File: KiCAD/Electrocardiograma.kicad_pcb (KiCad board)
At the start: 2 copper layers, 56.5 x 48.1 mm, 89 parts, among them J1 54-00174, J2 Conn_01x02_Pin, J3 USB_C_Receptacle_PowerOnly_6P, J4 Conn_01x02_Pin, J5 Conn_01x02_Pin, J6 Conn_01x04_Pin, U1 INA823DT, U2 ESP32-C3-WROOM-02, U3 TLV1117-33, U4 TLV4888, U5 TLV4888, U6 TLV1117-ADJ, U7 SC6038, U8 CH224K

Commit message: cambios de placa y esquematico
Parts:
- moved C25 48.1 mm to (199.2, 61.0)
- moved R45 48.1 mm to (210.1, 63.4)
- moved R47 48.1 mm to (210.1, 66.4)
- moved R48 48.1 mm to (210.1, 69.3)
- moved R49 48.1 mm to (210.1, 72.3)
- moved C22 33.2 mm to (204.2, 65.1)
- moved C24 33.2 mm to (204.2, 71.1)
- moved C20 33.2 mm to (204.3, 59.1)
- moved C21 33.2 mm to (204.2, 62.1)
- moved D6 33.2 mm to (195.3, 50.1)
- moved R42 33.2 mm to (195.3, 54.1)
- moved C23 33.2 mm to (204.2, 68.1)
- moved C26 33.2 mm to (204.2, 54.6)
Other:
- board size 56.5 x 48.1 mm -> 67 x 50 mm

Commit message: Falta por aprobar errores en la etapa de amplificación
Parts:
- added C27: 10nF, Capacitor_SMD:C_0805_2012Metric_Pad1.18x1.45mm_HandSolder, F.Cu at (215.5, 60.9)
- added C28: 10nF, Capacitor_SMD:C_0805_2012Metric_Pad1.18x1.45mm_HandSolder, F.Cu at (215.5, 63.9)
- added C29: 10nF, Capacitor_SMD:C_0805_2012Metric_Pad1.18x1.45mm_HandSolder, F.Cu at (215.5, 66.9)
- added C30: 10nF, Capacitor_SMD:C_0805_2012Metric_Pad1.18x1.45mm_HandSolder, F.Cu at (215.5, 69.9)
- added C31: 10nF, Capacitor_SMD:C_0805_2012Metric_Pad1.18x1.45mm_HandSolder, F.Cu at (215.5, 72.9)
- added R50: 120, Resistor_SMD:R_0805_2012Metric_Pad1.20x1.40mm_HandSolder, F.Cu at (220.3, 60.8)
- R10: value 22K -> 2K67
- R11: value 33K -> 4k
- R12, R34, R36: value 100K -> 1K
- R17, R21: value 27K -> 2K67
- R19, R20, R22, R23: value 100K -> 10K
- R24: value 33K -> 1K
- R25: value 330k -> 24k
- R4: value 330k -> 33k
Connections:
- C22 pad 1: /Leveled_Signal -> Net-(C22-Pad1)
- R36 pad 2: /Leveled_Signal -> Net-(C22-Pad1)
- U4 pad 14: /Leveled_Signal -> Net-(C22-Pad1)
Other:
- outline, holes or cut-outs redrawn

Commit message: route tracing
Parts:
- R11: footprint Resistor_SMD:R_0805_2012Metric_Pad1.20x1.40mm_HandSolder -> Resistor_SMD:R_0603_1608Metric_Pad0.98x0.95mm_HandSolder
- R25: value 24k -> 1k
- moved R50 86.4 mm to (157.8, 120.5), turned to 180 degrees
- moved C26 80.9 mm to (139.6, 103.4), turned to 180 degrees
- moved C31 78.4 mm to (153.2, 120.5)
- moved C22 68.7 mm to (163.6, 120.5)
- moved C25 59.1 mm to (168.7, 111.6), turned to -90 degrees
- moved D6 54.9 mm to (146.2, 74.8), turned to 0 degrees
- moved C27 52.3 mm to (178.3, 97.6), turned to 180 degrees
- moved R42 48.7 mm to (151.4, 75.2)
- moved C20 47.7 mm to (165.8, 87.3), turned to 90 degrees
- moved R45 44.8 mm to (178.3, 95.0), turned to 180 degrees
- moved C30 40.2 mm to (213.8, 110.0)
- moved C24 39.0 mm to (205.0, 110.1)
- moved R49 37.8 mm to (209.4, 110.1)
- moved C29 35.3 mm to (213.2, 102.1)
- moved C23 34.2 mm to (204.6, 102.3)
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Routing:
- net +6.1V: track 156.5 -> 90.1 mm, vias 5 -> 2
- net Net-(C20-Pad2): track 0.00 -> 30.0 mm, vias 0 -> 3
- net Net-(C22-Pad1): track 0.00 -> 21.6 mm, vias 0 -> 2
- net Net-(D6-A): track 0.00 -> 18.1 mm
- net Net-(U1--): track 15.8 -> 0.00 mm
- net -BATT_REG: track 25.5 -> 41.1 mm, vias 33 -> 28
- net Net-(U1-+): track 13.0 -> 0.00 mm
- net +BATT: track 18.7 -> 8.14 mm
- net +3.3V: track 134.3 -> 124.3 mm
- net Net-(U5A-+): track 25.0 -> 34.5 mm
- net Net-(U4A--): track 15.1 -> 6.55 mm
- net Net-(D6-K): track 0.00 -> 7.79 mm
- net GND: track 89.7 -> 96.9 mm, vias 7 -> 6
- net Net-(U4D--): track 15.1 -> 21.7 mm
- net Net-(U6-ADJ): track 7.10 -> 12.7 mm
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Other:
- board text removed: "Añadidos Capacitores de desacople"

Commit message: Update Electrocardiograma.kicad_pcb
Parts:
- D1: value D_TVS_Dual_AAC -> TVS
- moved C28 69.3 mm to (144.2, 101.4), turned to 90 degrees
- moved C29 60.0 mm to (153.3, 106.0)
- moved C21 59.6 mm to (145.3, 94.7), turned to 180 degrees
- moved R47 58.8 mm to (150.6, 92.1), turned to 180 degrees
- moved C23 46.8 mm to (157.8, 105.9)
- moved R48 46.7 mm to (162.2, 105.9)
- moved D6 15.8 mm to (162.0, 74.3)
- moved R10 4.11 mm to (150.6, 97.4)
- moved R11 1.51 mm to (150.6, 94.7)
- moved C5 1.14 mm to (145.3, 97.3)
- moved C8 0.92 mm to (145.3, 92.1)
- moved R25 0.85 mm to (162.2, 103.4)
- moved C11 0.84 mm to (157.8, 103.4)
- moved R20 0.84 mm to (153.3, 103.4)
- moved C15 0.60 mm to (153.5, 84.3)
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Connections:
- C26 pad 2: Net-(U6-ADJ) -> unconnected-(C26-Pad2)
- R31 pad 1: +6.1V -> unconnected-(R31-Pad1)
- R31 pad 2: Net-(U6-ADJ) -> unconnected-(R31-Pad2)
- R32 pad 1: Net-(U6-ADJ) -> unconnected-(R32-Pad1)
- R32 pad 2: -BATT_REG -> unconnected-(R32-Pad2)
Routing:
- net Net-(C11-Pad2): track 0.00 -> 18.0 mm, vias 0 -> 2
- net Net-(C21-Pad2): track 0.00 -> 16.6 mm
- net Net-(D6-A): track 18.1 -> 4.28 mm
- net GND: track 96.9 -> 104.7 mm, vias 6 -> 5
- net Net-(U5C-+): track 17.1 -> 12.9 mm, vias 0 -> 2
- net /N50Hz_out: track 16.8 -> 13.1 mm, vias 0 -> 2
- net /Sensing_Out: track 12.2 -> 8.89 mm
- net Net-(U5B--): track 10.3 -> 13.4 mm
- net Net-(U5C--): track 7.40 -> 10.2 mm
- net Net-(C11-Pad1): track 18.4 -> 15.7 mm, vias 0 -> 2
- net Net-(C5-Pad2): track 17.8 -> 19.6 mm
- net Net-(D6-K): track 7.79 -> 9.23 mm
- net Net-(U5D--): track 10.8 -> 10.0 mm
- net /LPF_out: track 18.8 -> 18.5 mm, vias 2 -> 0

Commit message: Update Electrocardiograma.kicad_pcb
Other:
- outline, holes or cut-outs redrawn
- board text removed: "Falso, debe sobresalir para igualar el grosor de la carcasa"

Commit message: Update Electrocardiograma.kicad_pcb
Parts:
- moved C30 43.6 mm to (170.7, 103.1), turned to -90 degrees
- moved R49 43.2 mm to (166.8, 103.4)
- moved C24 39.4 mm to (166.8, 100.7)
- moved R4 5.59 mm to (168.7, 116.6)
- moved R5 3.41 mm to (171.4, 111.6), turned to 90 degrees
- moved C14 3.31 mm to (166.8, 105.9), turned to 0 degrees
- moved R1 2.42 mm to (174.5, 107.1)
- moved R2 2.16 mm to (174.5, 102.5)
- moved R24 0.14 mm to (171.4, 116.6)
- moved R48 0.08 mm to (162.2, 105.9)
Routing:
- net GND: track 104.7 -> 136.0 mm, vias 5 -> 7
- net Net-(C24-Pad2): track 0.00 -> 14.8 mm
- net -BATT_REG: track 41.1 -> 27.6 mm, vias 28 -> 29
- net Net-(U4A-+): track 13.9 -> 2.30 mm, vias 2 -> 1
- net Net-(R2-Pad2): track 0.00 -> 5.29 mm
- net Net-(R1-Pad1): track 0.00 -> 5.28 mm
- net Net-(U4B--): track 8.65 -> 13.2 mm
- net +6.1V: track 90.1 -> 94.3 mm
- net Net-(C25-Pad1): track 8.32 -> 12.0 mm
- net Net-(U5D--): track 10.0 -> 12.5 mm
- net /Sensing_Out: track 8.89 -> 7.37 mm
- net Net-(U4D-+): track 21.3 -> 20.1 mm
- net Net-(J1-Pad2): track 4.47 -> 3.49 mm
- net Net-(U4A--): track 6.55 -> 7.34 mm

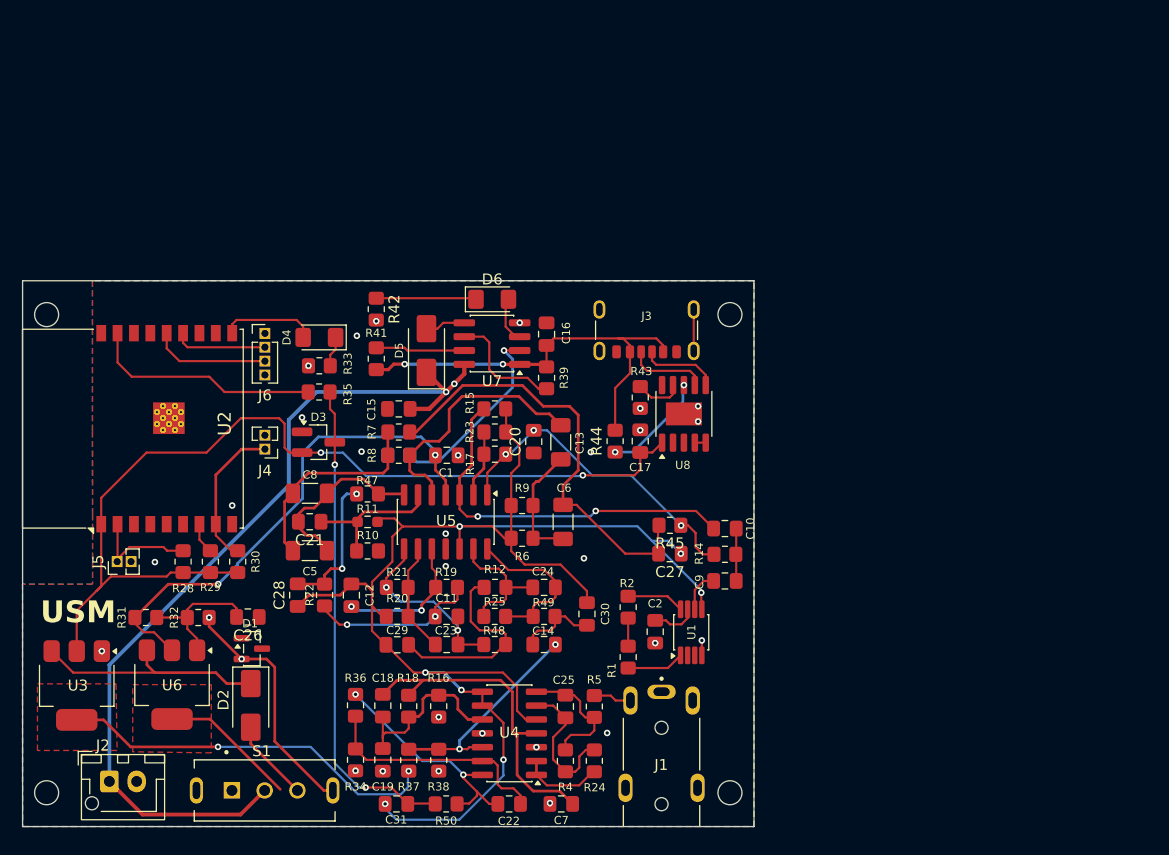
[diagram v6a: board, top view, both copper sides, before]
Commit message: Finished first PCB retracing
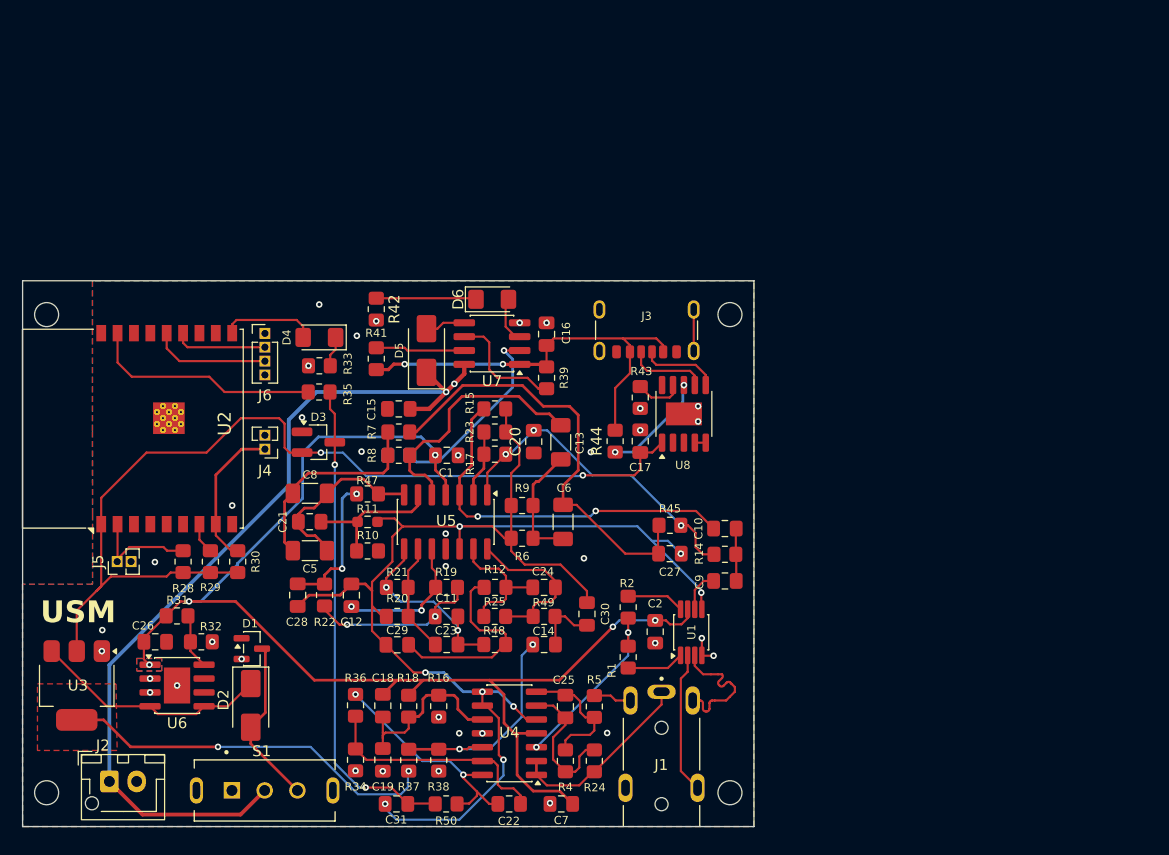
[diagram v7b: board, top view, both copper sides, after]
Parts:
- D1: value TVS -> D_TVS_Dual_AAC
- R31: value 120 -> 1k
- R32: value 470 -> 100
- U6: value TLV1117-ADJ -> ASPL4030-ADJW-R; footprint Package_TO_SOT_SMD:SOT-223-3_TabPin2 -> Package_SO:SOIC-8-1EP_3.9x4.9mm_P1.27mm_EP2.41x3.3mm
- moved C26 8.79 mm to (131.2, 105.7)
- moved R31 2.87 mm to (133.2, 103.3)
- moved R32 2.24 mm to (135.4, 105.7)
- moved U6 0.47 mm to (133.2, 109.7), turned to 0 degrees
- turned C14 to 180 degrees
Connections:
- C26 pad 2: unconnected-(C26-Pad2) -> +6.1V
- R31 pad 1: unconnected-(R31-Pad1) -> +6.1V
- R31 pad 2: unconnected-(R31-Pad2) -> Net-(U6-FB)
- R32 pad 1: unconnected-(R32-Pad1) -> Net-(U6-FB)
- R32 pad 2: unconnected-(R32-Pad2) -> -BATT_REG
- U6 pad 1: Net-(U6-ADJ) -> +6.1V
- U6 pad 2: +6.1V -> -BATT_REG
- U6 pad 3: Net-(D2-K) -> -BATT_REG
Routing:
- net +6.1V: track 94.3 -> 118.2 mm, vias 2 -> 5
- net -BATT_REG: track 27.6 -> 6.52 mm, vias 29 -> 37
- net Net-(U4A-+): track 2.30 -> 16.3 mm, vias 1 -> 2
- net Net-(U1--): track 0.00 -> 13.0 mm
- net Net-(U1-+): track 0.00 -> 12.9 mm
- net Net-(U6-ADJ): track 12.7 -> 0.00 mm
- net Net-(U4A--): track 7.34 -> 17.2 mm
- net +BATT: track 8.14 -> 16.0 mm
- net GND: track 136.0 -> 128.8 mm, vias 7 -> 8
- net Net-(U6-FB): track 0.00 -> 5.08 mm
- net /Sensing_Out: track 7.37 -> 5.85 mm
- net Net-(U4D-+): track 20.1 -> 20.8 mm
- added copper zone on B.Cu, net +6.1V

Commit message: Retiro de mounting holes
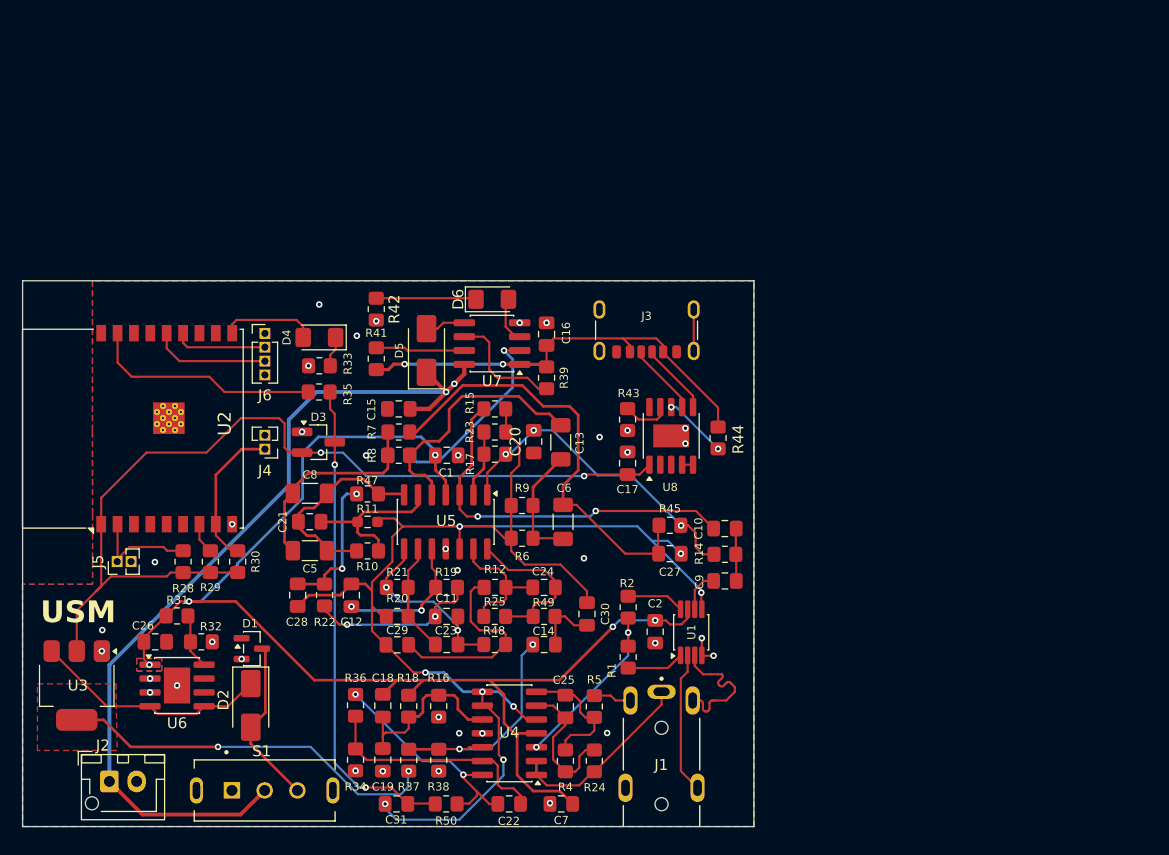
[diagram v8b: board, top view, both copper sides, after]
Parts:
- moved R44 9.43 mm to (182.7, 87.0)
- moved C17 2.33 mm to (174.4, 89.3)
- moved R43 2.33 mm to (174.4, 85.3)
- moved U8 2.33 mm to (178.4, 86.8)
- turned R10 to 180 degrees
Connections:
- U6 pad 9: -BATT_REG -> (no net)
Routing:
- net Net-(U8-VBUS): track 9.71 -> 5.87 mm
- net +3.3V: track 124.3 -> 121.4 mm
- net Net-(C21-Pad2): track 16.6 -> 19.3 mm
- net Net-(U5B--): track 13.4 -> 15.0 mm
- net /Vbus: track 39.1 -> 40.4 mm
- net Net-(J3-CC2): track 7.39 -> 6.62 mm
- net Net-(J3-CC1): track 7.19 -> 6.62 mm
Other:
- outline, holes or cut-outs redrawn
